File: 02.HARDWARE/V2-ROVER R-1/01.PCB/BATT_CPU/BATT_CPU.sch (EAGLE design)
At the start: 90 parts, among them J1 DF40C_2.0_-20DS-0.4V_51_, Q1 BSS84W-7-F, Q2 BSS84W-7-F, Q3 2N7002PW, Q4 2N7002PW, Q5 BSS84W-7-F, U1 ATSAMD21G18_QFN, U3 TPS78230DDCR, U6 MAX9062EUK+T, U8 SN74LVC1G19DBVR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

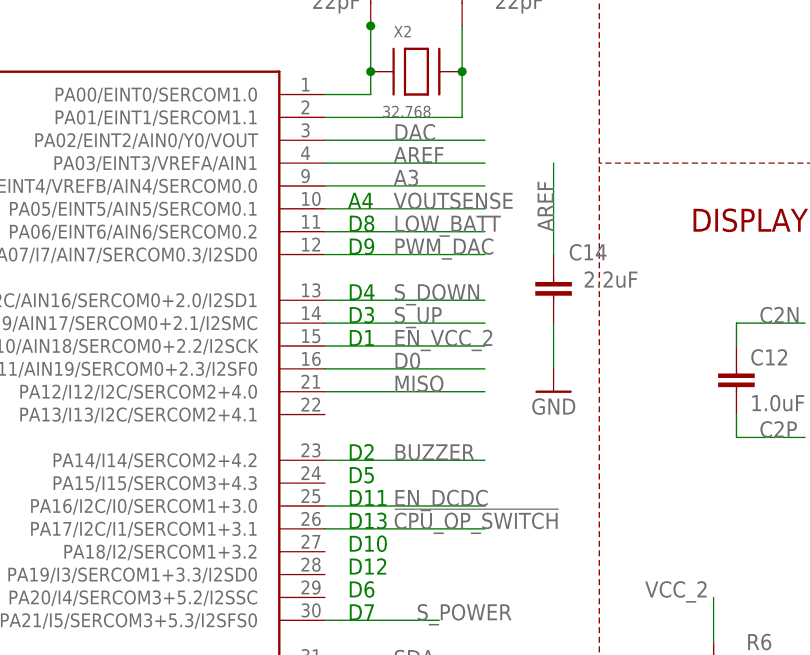
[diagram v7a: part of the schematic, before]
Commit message: Union de salidas digitales a SWD. CPU
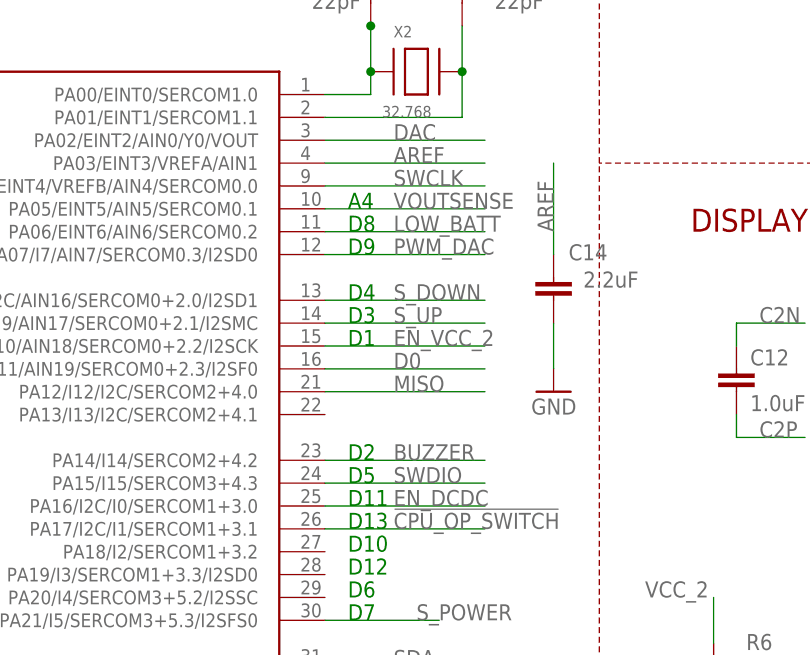
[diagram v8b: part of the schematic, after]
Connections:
- removed net A3: U1.PA04/EINT4/VREFB/AIN4/SERCOM0.0
- net SWCLK: now also U1.PA04/EINT4/VREFB/AIN4/SERCOM0.0
- net SWDIO: now also U1.PA15/I15/SERCOM3+4.3
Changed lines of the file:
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@@
-</segment>
-</net>
-<net name="A3" class="0">
-<segment>
-<pinref part="U1" gate="G$1" pin="PA04/EINT4/VREFB/AIN4/SERCOM0.0"/>
-<wire x1="104.14" y1="86.36" x2="121.92" y2="86.36" width="0.1524" layer="91"/>
-<label x="111.76" y="86.36" size="1.778" layer="95"/>
 </segment>
 </net>
@@
 <label x="294.64" y="149.86" size="1.778" layer="95"/>
 </segment>
+<segment>
+<pinref part="U1" gate="G$1" pin="PA04/EINT4/VREFB/AIN4/SERCOM0.0"/>
+<wire x1="104.14" y1="86.36" x2="121.92" y2="86.36" width="0.1524" layer="91"/>
+<label x="111.76" y="86.36" size="1.778" layer="95"/>
+</segment>
 </net>
 <net name="SWDIO" class="0">
@@
 <label x="294.64" y="147.32" size="1.778" layer="95"/>
 </segment>
+<segment>
+<pinref part="U1" gate="G$1" pin="PA15/I15/SERCOM3+4.3"/>
+<wire x1="104.14" y1="53.34" x2="121.92" y2="53.34" width="0.1524" layer="91"/>
+<label x="111.76" y="53.34" size="1.778" layer="95"/>
+</segment>
 </net>
